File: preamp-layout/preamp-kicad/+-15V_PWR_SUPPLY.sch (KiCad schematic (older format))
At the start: 33 parts, among them J1 Screw_Terminal_01x02, J2 Conn_01x03_Female, J3 Conn_01x03_Female, J4 Conn_01x03_Female, T1 Transformer_1P_1S, U1 L7805, U2 LM7905_TO220

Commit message: AC PCB Update
Removed Switch symbol from PCB, moved to main sheet. Started playing with footprint assignment. Other minor updates.
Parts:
- renumbered J1 to J5, J2 to J6, J3 to J7, J4 to J8
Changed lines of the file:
@@
 $EndDescr
 $Comp
-L Connector:Screw_Terminal_01x02 J1
+L Connector:Screw_Terminal_01x02 J5
 U 1 1 5F8FF1B9
 P 1200 3150
-F 0 "J1" H 1118 3275 50  0000 C CNN
+F 0 "J5" H 1118 3275 50  0000 C CNN
 F 1 "Screw_Terminal_01x02" H 1118 2916 50  0001 C CNN
 F 2 "" H 1200 3150 50  0001 C CNN
@@
 AR Path="/5E2D8DA2/647A815C" Ref="J?"  Part="1"
 AR Path="/6009D432/647A815C" Ref="J?"  Part="1"
-AR Path="/5E27B612/647A815C" Ref="J2"  Part="1"
-F 0 "J2" H 2228 5826 50  0000 L CNN
+AR Path="/5E27B612/647A815C" Ref="J6"  Part="1"
+F 0 "J6" H 2228 5826 50  0000 L CNN
 F 1 "Conn_01x03_Female" H 2228 5735 50  0001 L CNN
 F 2 "" H 2200 5800 50  0001 C CNN
@@
 AR Path="/5E2D8DA2/647B6C33" Ref="J?"  Part="1"
 AR Path="/6009D432/647B6C33" Ref="J?"  Part="1"
-AR Path="/5E27B612/647B6C33" Ref="J3"  Part="1"
-F 0 "J3" H 2228 6426 50  0000 L CNN
+AR Path="/5E27B612/647B6C33" Ref="J7"  Part="1"
+F 0 "J7" H 2228 6426 50  0000 L CNN
 F 1 "Conn_01x03_Female" H 2228 6335 50  0001 L CNN
 F 2 "" H 2200 6400 50  0001 C CNN
@@
 AR Path="/5E2D8DA2/647BAB03" Ref="J?"  Part="1"
 AR Path="/6009D432/647BAB03" Ref="J?"  Part="1"
-AR Path="/5E27B612/647BAB03" Ref="J4"  Part="1"
-F 0 "J4" H 2228 7026 50  0000 L CNN
+AR Path="/5E27B612/647BAB03" Ref="J8"  Part="1"
+F 0 "J8" H 2228 7026 50  0000 L CNN
 F 1 "Conn_01x03_Female" H 2228 6935 50  0001 L CNN
 F 2 "" H 2200 7000 50  0001 C CNN
@@
 $EndComp
 $Comp
-L power:PWR_FLAG #FLG0101
+L power:PWR_FLAG #FLG01
 U 1 1 65A127EB
 P 6800 2050
-F 0 "#FLG0101" H 6800 2125 50  0001 C CNN
+F 0 "#FLG01" H 6800 2125 50  0001 C CNN
 F 1 "PWR_FLAG" H 6800 2223 50  0000 C CNN
 F 2 "" H 6800 2050 50  0001 C CNN
@@
 $EndComp
 $Comp
-L power:PWR_FLAG #FLG0102
+L power:PWR_FLAG #FLG02
 U 1 1 65A13199
 P 6800 4450
-F 0 "#FLG0102" H 6800 4525 50  0001 C CNN
+F 0 "#FLG02" H 6800 4525 50  0001 C CNN
 F 1 "PWR_FLAG" H 6800 4623 50  0000 C CNN
 F 2 "" H 6800 4450 50  0001 C CNN
@@
 	8100 2700 8100 2350
 $Comp
-L power:PWR_FLAG #FLG0103
+L power:PWR_FLAG #FLG03
 U 1 1 65AD6168
 P 8350 2700
-F 0 "#FLG0103" H 8350 2775 50  0001 C CNN
+F 0 "#FLG03" H 8350 2775 50  0001 C CNN
 F 1 "PWR_FLAG" H 8350 2873 50  0000 C CNN
 F 2 "" H 8350 2700 50  0001 C CNN
@@
 Connection ~ 8350 3800
 $Comp
-L power:PWR_FLAG #FLG0104
+L power:PWR_FLAG #FLG04
 U 1 1 65ADBCDE
 P 8350 3800
-F 0 "#FLG0104" H 8350 3875 50  0001 C CNN
+F 0 "#FLG04" H 8350 3875 50  0001 C CNN
 F 1 "PWR_FLAG" H 8350 3973 50  0000 C CNN
 F 2 "" H 8350 3800 50  0001 C CNN

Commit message: Initial Footprint Assignment
Assigned footprints to SMT resistors, pin headers, screw terminals, LEDs, DIP-8 ICs
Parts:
- D2, D3: footprint (none) -> LED_SMD:LED_1206_3216Metric_Pad1.42x1.75mm_HandSolder
- F2: value Fuse -> 500mA
- J5: footprint (none) -> TerminalBlock_Phoenix:TerminalBlock_Phoenix_PT-1,5-2-5.0-H_1x02_P5.00mm_Horizontal
- J6, J7, J8: footprint (none) -> Connector_PinHeader_2.54mm:PinHeader_1x03_P2.54mm_Vertical
- R2, R3: footprint (none) -> Resistor_SMD:R_1206_3216Metric_Pad1.42x1.75mm_HandSolder
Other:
- moved on the sheet: J5
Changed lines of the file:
@@
 L Connector:Screw_Terminal_01x02 J5
 U 1 1 5F8FF1B9
-P 1200 3150
-F 0 "J5" H 1118 3275 50  0000 C CNN
-F 1 "Screw_Terminal_01x02" H 1118 2916 50  0001 C CNN
-F 2 "" H 1200 3150 50  0001 C CNN
-F 3 "~" H 1200 3150 50  0001 C CNN
-	1    1200 3150
+P 1300 3150
+F 0 "J5" H 1218 3275 50  0000 C CNN
+F 1 "Screw_Terminal_01x02" H 1218 2916 50  0001 C CNN
+F 2 "TerminalBlock_Phoenix:TerminalBlock_Phoenix_PT-1,5-2-5.0-H_1x02_P5.00mm_Horizontal" H 1300 3150 50  0001 C CNN
+F 3 "~" H 1300 3150 50  0001 C CNN
+	1    1300 3150
 	-1   0    0    -1
 $EndComp
 Wire Wire Line
-	1400 3150 1500 3150
-Wire Wire Line
 	1800 3150 1800 3000
 Wire Wire Line
-	1400 3250 1600 3250
-Wire Wire Line
 	1800 3250 1800 3400
-Text HLabel 1500 3400 3    50   UnSpc ~ 0
+Text HLabel 1650 3050 1    50   UnSpc ~ 0
 AC+
-Text HLabel 1600 3400 3    50   UnSpc ~ 0
+Text HLabel 1650 3350 3    50   UnSpc ~ 0
 AC-
-Wire Wire Line
-	1500 3400 1500 3150
-Connection ~ 1500 3150
-Wire Wire Line
-	1500 3150 1800 3150
-Wire Wire Line
-	1600 3400 1600 3250
-Connection ~ 1600 3250
-Wire Wire Line
-	1600 3250 1800 3250
 Text GLabel 4550 6200 1    50   UnSpc ~ 0
 +15V
@@
 F 0 "R2" V 4343 6450 50  0000 C CNN
 F 1 "10K" V 4434 6450 50  0000 C CNN
-F 2 "" V 4480 6450 50  0001 C CNN
+F 2 "Resistor_SMD:R_1206_3216Metric_Pad1.42x1.75mm_HandSolder" V 4480 6450 50  0001 C CNN
 F 3 "~" H 4550 6450 50  0001 C CNN
 	1    4550 6450
@@
 F 0 "D2" V 4589 6733 50  0000 R CNN
 F 1 "LED" V 4498 6733 50  0000 R CNN
-F 2 "" H 4550 6850 50  0001 C CNN
+F 2 "LED_SMD:LED_1206_3216Metric_Pad1.42x1.75mm_HandSolder" H 4550 6850 50  0001 C CNN
 F 3 "~" H 4550 6850 50  0001 C CNN
 	1    4550 6850
@@
 F 0 "R3" V 4893 6450 50  0000 C CNN
 F 1 "10K" V 4984 6450 50  0000 C CNN
-F 2 "" V 5030 6450 50  0001 C CNN
+F 2 "Resistor_SMD:R_1206_3216Metric_Pad1.42x1.75mm_HandSolder" V 5030 6450 50  0001 C CNN
 F 3 "~" H 5100 6450 50  0001 C CNN
 	1    5100 6450
@@
 F 0 "D3" V 5139 6733 50  0000 R CNN
 F 1 "LED" V 5048 6733 50  0000 R CNN
-F 2 "" H 5100 6850 50  0001 C CNN
+F 2 "LED_SMD:LED_1206_3216Metric_Pad1.42x1.75mm_HandSolder" H 5100 6850 50  0001 C CNN
 F 3 "~" H 5100 6850 50  0001 C CNN
 	1    5100 6850
@@
 AR Path="/5E27B612/60029A0D" Ref="F2"  Part="1"
 F 0 "F2" V 2603 3000 50  0000 C CNN
-F 1 "Fuse" V 2694 3000 50  0000 C CNN
+F 1 "500mA" V 2694 3000 50  0000 C CNN
 F 2 "" V 2730 3000 50  0001 C CNN
 F 3 "~" H 2800 3000 50  0001 C CNN
@@
 U 1 1 5FD657B8
 P 2200 3200
-F 0 "T1" H 2200 3581 50  0000 C CNN
-F 1 "Transformer_1P_1S" H 2200 3490 50  0000 C CNN
+F 0 "T1" H 2200 3489 50  0000 C CNN
+F 1 "Transformer_1P_1S" H 2200 3490 50  0001 C CNN
 F 2 "" H 2200 3200 50  0001 C CNN
 F 3 "~" H 2200 3200 50  0001 C CNN
@@
 F 0 "J6" H 2228 5826 50  0000 L CNN
 F 1 "Conn_01x03_Female" H 2228 5735 50  0001 L CNN
-F 2 "" H 2200 5800 50  0001 C CNN
+F 2 "Connector_PinHeader_2.54mm:PinHeader_1x03_P2.54mm_Vertical" H 2200 5800 50  0001 C CNN
 F 3 "~" H 2200 5800 50  0001 C CNN
 	1    2200 5800
@@
 F 0 "J7" H 2228 6426 50  0000 L CNN
 F 1 "Conn_01x03_Female" H 2228 6335 50  0001 L CNN
-F 2 "" H 2200 6400 50  0001 C CNN
+F 2 "Connector_PinHeader_2.54mm:PinHeader_1x03_P2.54mm_Vertical" H 2200 6400 50  0001 C CNN
 F 3 "~" H 2200 6400 50  0001 C CNN
 	1    2200 6400
@@
 F 0 "J8" H 2228 7026 50  0000 L CNN
 F 1 "Conn_01x03_Female" H 2228 6935 50  0001 L CNN
-F 2 "" H 2200 7000 50  0001 C CNN
+F 2 "Connector_PinHeader_2.54mm:PinHeader_1x03_P2.54mm_Vertical" H 2200 7000 50  0001 C CNN
 F 3 "~" H 2200 7000 50  0001 C CNN
 	1    2200 7000
@@
 	-1   0    0    1
 $EndComp
+Wire Wire Line
+	1500 3150 1650 3150
+Wire Wire Line
+	1500 3250 1650 3250
+Wire Wire Line
+	1650 3050 1650 3150
+Connection ~ 1650 3150
+Wire Wire Line
+	1650 3150 1800 3150
+Wire Wire Line
+	1650 3250 1650 3350
+Connection ~ 1650 3250
+Wire Wire Line
+	1650 3250 1800 3250
 $EndSCHEMATC

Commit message: BOM update
Minor changes to schematic, value changes and footprint entry. BOM updated with parts sourcing
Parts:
- D4, D5: value D -> SM4001; footprint (none) -> Diode_SMD:D_SOD-123F
- D6, D7: value 1N4004 -> SM4001; footprint (none) -> Diode_SMD:D_SOD-123F
- R2, R3: value 10K -> 430
- R6, R7: value 240R 1% -> 240R
- RV1, RV2: value R_POT_US -> 5k
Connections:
- wire segments 124 -> 122
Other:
- moved on the sheet: D1, F2, J5
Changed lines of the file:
@@
 L Connector:Screw_Terminal_01x02 J5
 U 1 1 5F8FF1B9
-P 1300 3150
-F 0 "J5" H 1218 3275 50  0000 C CNN
-F 1 "Screw_Terminal_01x02" H 1218 2916 50  0001 C CNN
-F 2 "TerminalBlock_Phoenix:TerminalBlock_Phoenix_PT-1,5-2-5.0-H_1x02_P5.00mm_Horizontal" H 1300 3150 50  0001 C CNN
-F 3 "~" H 1300 3150 50  0001 C CNN
-	1    1300 3150
+P 900 3150
+F 0 "J5" H 818 3275 50  0000 C CNN
+F 1 "Screw_Terminal_01x02" H 818 2916 50  0001 C CNN
+F 2 "TerminalBlock_Phoenix:TerminalBlock_Phoenix_PT-1,5-2-5.0-H_1x02_P5.00mm_Horizontal" H 900 3150 50  0001 C CNN
+F 3 "~" H 900 3150 50  0001 C CNN
+	1    900  3150
 	-1   0    0    -1
 $EndComp
@@
 Wire Wire Line
 	1800 3250 1800 3400
-Text HLabel 1650 3050 1    50   UnSpc ~ 0
+Text HLabel 1250 3050 1    50   UnSpc ~ 0
 AC+
-Text HLabel 1650 3350 3    50   UnSpc ~ 0
+Text HLabel 1250 3350 3    50   UnSpc ~ 0
 AC-
 Text GLabel 4550 6200 1    50   UnSpc ~ 0
@@
 AR Path="/5FFF1130" Ref="R?"  Part="1"
 AR Path="/5E27B612/5FFF1130" Ref="R2"  Part="1"
-F 0 "R2" V 4343 6450 50  0000 C CNN
-F 1 "10K" V 4434 6450 50  0000 C CNN
+F 0 "R2" H 4620 6496 50  0000 L CNN
+F 1 "430" H 4620 6405 50  0000 L CNN
 F 2 "Resistor_SMD:R_1206_3216Metric_Pad1.42x1.75mm_HandSolder" V 4480 6450 50  0001 C CNN
 F 3 "~" H 4550 6450 50  0001 C CNN
@@
 AR Path="/5FFF1146" Ref="R?"  Part="1"
 AR Path="/5E27B612/5FFF1146" Ref="R3"  Part="1"
-F 0 "R3" V 4893 6450 50  0000 C CNN
-F 1 "10K" V 4984 6450 50  0000 C CNN
+F 0 "R3" H 5170 6496 50  0000 L CNN
+F 1 "430" H 5170 6405 50  0000 L CNN
 F 2 "Resistor_SMD:R_1206_3216Metric_Pad1.42x1.75mm_HandSolder" V 5030 6450 50  0001 C CNN
 F 3 "~" H 5100 6450 50  0001 C CNN
@@
 AR Path="/5E2D8DA2/5FFF114C" Ref="D?"  Part="1"
 AR Path="/5E27B612/5FFF114C" Ref="D3"  Part="1"
-F 0 "D3" V 5139 6733 50  0000 R CNN
-F 1 "LED" V 5048 6733 50  0000 R CNN
+F 0 "D3" V 5047 6928 50  0000 L CNN
+F 1 "LED" V 5138 6928 50  0000 L CNN
 F 2 "LED_SMD:LED_1206_3216Metric_Pad1.42x1.75mm_HandSolder" H 5100 6850 50  0001 C CNN
 F 3 "~" H 5100 6850 50  0001 C CNN
@@
 L Device:Fuse F?
 U 1 1 60029A0D
-P 2800 3000
+P 1550 3150
 AR Path="/5E26F6FE/60029A0D" Ref="F?"  Part="1"
 AR Path="/5E27B612/60029A0D" Ref="F2"  Part="1"
-F 0 "F2" V 2603 3000 50  0000 C CNN
-F 1 "500mA" V 2694 3000 50  0000 C CNN
-F 2 "" V 2730 3000 50  0001 C CNN
-F 3 "~" H 2800 3000 50  0001 C CNN
-	1    2800 3000
+F 0 "F2" V 1353 3150 50  0000 C CNN
+F 1 "500mA" V 1444 3150 50  0000 C CNN
+F 2 "" V 1480 3150 50  0001 C CNN
+F 3 "~" H 1550 3150 50  0001 C CNN
+	1    1550 3150
 	0    1    1    0
 $EndComp
-Wire Wire Line
-	2600 3000 2650 3000
-Wire Wire Line
-	2600 3400 2650 3400
 $Comp
 L Diode_Bridge:DF02M D1
 U 1 1 5FBF248C
-P 3300 3200
-F 0 "D1" H 3644 3246 50  0000 L CNN
-F 1 "DF02M" H 3644 3155 50  0000 L CNN
-F 2 "Diode_THT:Diode_Bridge_DIP-4_W7.62mm_P5.08mm" H 3450 3325 50  0001 L CNN
-F 3 "http://www.vishay.com/docs/88571/dfm.pdf" H 3300 3200 50  0001 C CNN
-	1    3300 3200
-	1    0    0    -1
-$EndComp
-Wire Wire Line
-	2650 3400 2650 3550
-Wire Wire Line
-	2650 3550 3300 3550
-Wire Wire Line
-	3300 3550 3300 3500
-Wire Wire Line
-	2950 3000 3000 3000
-Wire Wire Line
-	3000 3000 3000 2850
-Wire Wire Line
-	3000 2850 3300 2850
-Wire Wire Line
-	3300 2850 3300 2900
-Wire Wire Line
-	3000 3200 3000 3650
-Wire Wire Line
-	3600 3200 3600 3650
-Text Label 3000 3650 3    50   ~ 0
+P 3150 3200
+F 0 "D1" H 3494 3246 50  0000 L CNN
+F 1 "DF02M" H 3494 3155 50  0000 L CNN
+F 2 "Diode_THT:Diode_Bridge_DIP-4_W7.62mm_P5.08mm" H 3300 3325 50  0001 L CNN
+F 3 "http://www.vishay.com/docs/88571/dfm.pdf" H 3150 3200 50  0001 C CNN
+	1    3150 3200
+	1    0    0    -1
+$EndComp
+Text Label 2850 3800 3    50   ~ 0
 rectified_-
-Text Label 3600 3650 3    50   ~ 0
+Text Label 3450 3800 3    50   ~ 0
 rectified_+
 $Comp
@@
 AR Path="/5E27B612/5FE3F8A6" Ref="D4"  Part="1"
 AR Path="/5E5EF2D4/5FE3F8A6" Ref="D?"  Part="1"
-F 0 "D4" V 8054 1679 50  0000 L CNN
-F 1 "D" V 8145 1679 50  0000 L CNN
-F 2 "" H 8100 1600 50  0001 C CNN
+F 0 "D4" H 8100 1816 50  0000 C CNN
+F 1 "SM4001" H 8100 1725 50  0000 C CNN
+F 2 "Diode_SMD:D_SOD-123F" H 8100 1600 50  0001 C CNN
 F 3 "~" H 8100 1600 50  0001 C CNN
 	1    8100 1600
@@
 AR Path="/5E5EF2D4/5FE3F8AD" Ref="R?"  Part="1"
 F 0 "R6" H 8670 2696 50  0000 L CNN
-F 1 "240R 1%" H 8670 2605 50  0000 L CNN
+F 1 "240R" H 8670 2605 50  0000 L CNN
 F 2 "" V 8530 2650 50  0001 C CNN
 F 3 "~" H 8600 2650 50  0001 C CNN
@@
 AR Path="/5E27B612/5FE3F8C5" Ref="C6"  Part="1"
 AR Path="/5E5EF2D4/5FE3F8C5" Ref="C?"  Part="1"
-F 0 "C6" H 7615 2396 50  0000 L CNN
-F 1 "100nF 35V" H 7615 2305 50  0000 L CNN
+F 0 "C6" H 7386 2396 50  0000 R CNN
+F 1 "100nF 35V" H 7386 2305 50  0000 R CNN
 F 2 "" H 7538 2200 50  0001 C CNN
 F 3 "~" H 7500 2350 50  0001 C CNN
@@
 AR Path="/5E5EF2D4/5FE3F900" Ref="RV?"  Part="1"
 AR Path="/5E27B612/5FE3F900" Ref="RV1"  Part="1"
-F 0 "RV1" H 8033 2996 50  0000 R CNN
-F 1 "R_POT_US" H 8033 2905 50  0000 R CNN
+F 0 "RV1" H 8032 2996 50  0000 R CNN
+F 1 "5k" H 8032 2905 50  0000 R CNN
 F 2 "" H 8100 2950 50  0001 C CNN
 F 3 "~" H 8100 2950 50  0001 C CNN
@@
 AR Path="/5E5EF2D4/5FE3F90F" Ref="D?"  Part="1"
 F 0 "D6" V 9104 2729 50  0000 L CNN
-F 1 "1N4004" V 9195 2729 50  0000 L CNN
-F 2 "" H 9150 2650 50  0001 C CNN
+F 1 "SM4001" V 9195 2729 50  0000 L CNN
+F 2 "Diode_SMD:D_SOD-123F" H 9150 2650 50  0001 C CNN
 F 3 "~" H 9150 2650 50  0001 C CNN
 	1    9150 2650
@@
 AR Path="/5E27B612/5FE3F923" Ref="C9"  Part="1"
 AR Path="/5E5EF2D4/5FE3F923" Ref="C?"  Part="1"
-F 0 "C9" H 9765 3896 50  0000 L CNN
-F 1 "100nF 35V" H 9765 3805 50  0000 L CNN
+F 0 "C9" H 9765 3804 50  0000 L CNN
+F 1 "100nF 35V" H 9765 3895 50  0000 L CNN
 F 2 "" H 9688 3700 50  0001 C CNN
 F 3 "~" H 9650 3850 50  0001 C CNN
@@
 AR Path="/5E27B612/5FE3F929" Ref="D5"  Part="1"
 AR Path="/5E5EF2D4/5FE3F929" Ref="D?"  Part="1"
-F 0 "D5" V 8054 4979 50  0000 L CNN
-F 1 "D" V 8145 4979 50  0000 L CNN
-F 2 "" H 8100 4900 50  0001 C CNN
+F 0 "D5" H 8100 4776 50  0000 C CNN
+F 1 "SM4001" H 8100 4685 50  0000 C CNN
+F 2 "Diode_SMD:D_SOD-123F" H 8100 4900 50  0001 C CNN
 F 3 "~" H 8100 4900 50  0001 C CNN
 	1    8100 4900
@@
 AR Path="/5E27B612/5FE3F930" Ref="R7"  Part="1"
 AR Path="/5E5EF2D4/5FE3F930" Ref="R?"  Part="1"
-F 0 "R7" H 8670 3896 50  0000 L CNN
-F 1 "240R 1%" H 8670 3805 50  0000 L CNN
+F 0 "R7" H 8670 3804 50  0000 L CNN
+F 1 "240R" H 8670 3895 50  0000 L CNN
 F 2 "" V 8530 3850 50  0001 C CNN
 F 3 "~" H 8600 3850 50  0001 C CNN
@@
 AR Path="/5E27B612/5FE3F93A" Ref="R5"  Part="1"
 AR Path="/5E5EF2D4/5FE3F93A" Ref="R?"  Part="1"
-F 0 "R5" V 6193 4450 50  0000 C CNN
-F 1 "10R 1W" V 6284 4450 50  0000 C CNN
+F 0 "R5" V 6607 4450 50  0000 C CNN
+F 1 "10R 1W" V 6516 4450 50  0000 C CNN
 F 2 "" V 6330 4450 50  0001 C CNN
 F 3 "~" H 6400 4450 50  0001 C CNN
@@
 AR Path="/5E5EF2D4/5FE3F975" Ref="RV?"  Part="1"
 AR Path="/5E27B612/5FE3F975" Ref="RV2"  Part="1"
-F 0 "RV2" H 8033 3596 50  0000 R CNN
-F 1 "R_POT_US" H 8033 3505 50  0000 R CNN
+F 0 "RV2" H 8032 3504 50  0000 R CNN
+F 1 "5k" H 8032 3595 50  0000 R CNN
 F 2 "" H 8100 3550 50  0001 C CNN
 F 3 "~" H 8100 3550 50  0001 C CNN
@@
 AR Path="/5E5EF2D4/5FE3F992" Ref="D?"  Part="1"
 F 0 "D7" V 9104 3771 50  0000 R CNN
-F 1 "1N4004" V 9195 3771 50  0000 R CNN
-F 2 "" H 9150 3850 50  0001 C CNN
+F 1 "SM4001" V 9195 3771 50  0000 R CNN
+F 2 "Diode_SMD:D_SOD-123F" H 9150 3850 50  0001 C CNN
 F 3 "~" H 9150 3850 50  0001 C CNN
 	1    9150 3850
@@
 AR Path="/6009D432/647A815C" Ref="J?"  Part="1"
 AR Path="/5E27B612/647A815C" Ref="J6"  Part="1"
-F 0 "J6" H 2228 5826 50  0000 L CNN
+F 0 "J6" H 2228 5780 50  0000 L CNN
 F 1 "Conn_01x03_Female" H 2228 5735 50  0001 L CNN
 F 2 "Connector_PinHeader_2.54mm:PinHeader_1x03_P2.54mm_Vertical" H 2200 5800 50  0001 C CNN
@@
 AR Path="/6009D432/647B6C33" Ref="J?"  Part="1"
 AR Path="/5E27B612/647B6C33" Ref="J7"  Part="1"
-F 0 "J7" H 2228 6426 50  0000 L CNN
+F 0 "J7" H 2228 6380 50  0000 L CNN
 F 1 "Conn_01x03_Female" H 2228 6335 50  0001 L CNN
 F 2 "Connector_PinHeader_2.54mm:PinHeader_1x03_P2.54mm_Vertical" H 2200 6400 50  0001 C CNN
@@
 AR Path="/6009D432/647BAB03" Ref="J?"  Part="1"
 AR Path="/5E27B612/647BAB03" Ref="J8"  Part="1"
-F 0 "J8" H 2228 7026 50  0000 L CNN
+F 0 "J8" H 2228 6980 50  0000 L CNN
 F 1 "Conn_01x03_Female" H 2228 6935 50  0001 L CNN
 F 2 "Connector_PinHeader_2.54mm:PinHeader_1x03_P2.54mm_Vertical" H 2200 7000 50  0001 C CNN
@@
 AR Path="/5E27B612/64A0321E" Ref="#PWR06"  Part="1"
 F 0 "#PWR06" H 1900 6750 50  0001 C CNN
-F 1 "GND" H 1905 6827 50  0000 C CNN
+F 1 "GND" V 1905 6872 50  0000 R CNN
 F 2 "" H 1900 7000 50  0001 C CNN
 F 3 "" H 1900 7000 50  0001 C CNN
@@
 AR Path="/5E27B612/64A1966F" Ref="#PWR05"  Part="1"
 F 0 "#PWR05" H 1900 6150 50  0001 C CNN
-F 1 "GND" H 1905 6227 50  0000 C CNN
+F 1 "GND" V 1905 6272 50  0000 R CNN
 F 2 "" H 1900 6400 50  0001 C CNN
 F 3 "" H 1900 6400 50  0001 C CNN
@@
 AR Path="/5E27B612/64A1D9A5" Ref="#PWR04"  Part="1"
 F 0 "#PWR04" H 1900 5550 50  0001 C CNN
-F 1 "GND" H 1905 5627 50  0000 C CNN
+F 1 "GND" V 1905 5672 50  0000 R CNN
 F 2 "" H 1900 5800 50  0001 C CNN
 F 3 "" H 1900 5800 50  0001 C CNN
@@
 $EndComp
 Wire Wire Line
-	1500 3150 1650 3150
-Wire Wire Line
-	1500 3250 1650 3250
-Wire Wire Line
-	1650 3050 1650 3150
-Connection ~ 1650 3150
-Wire Wire Line
-	1650 3150 1800 3150
-Wire Wire Line
-	1650 3250 1650 3350
-Connection ~ 1650 3250
-Wire Wire Line
-	1650 3250 1800 3250
+	1100 3150 1250 3150
+Wire Wire Line
+	1100 3250 1250 3250
+Wire Wire Line
+	1250 3050 1250 3150
+Connection ~ 1250 3150
+Wire Wire Line
+	1250 3250 1250 3350
+Connection ~ 1250 3250
+Wire Wire Line
+	1250 3150 1400 3150
+Wire Wire Line
+	1250 3250 1800 3250
+Wire Wire Line
+	1700 3150 1800 3150
+Wire Wire Line
+	3150 2900 3150 2800
+Wire Wire Line
+	3150 2800 2600 2800
+Wire Wire Line
+	2600 2800 2600 3000
+Wire Wire Line
+	2600 3650 2600 3400
+Wire Wire Line
+	3150 3500 3150 3650
+Wire Wire Line
+	2600 3650 3150 3650
+Wire Wire Line
+	2850 3800 2850 3200
+Wire Wire Line
+	3450 3200 3450 3800
 $EndSCHEMATC

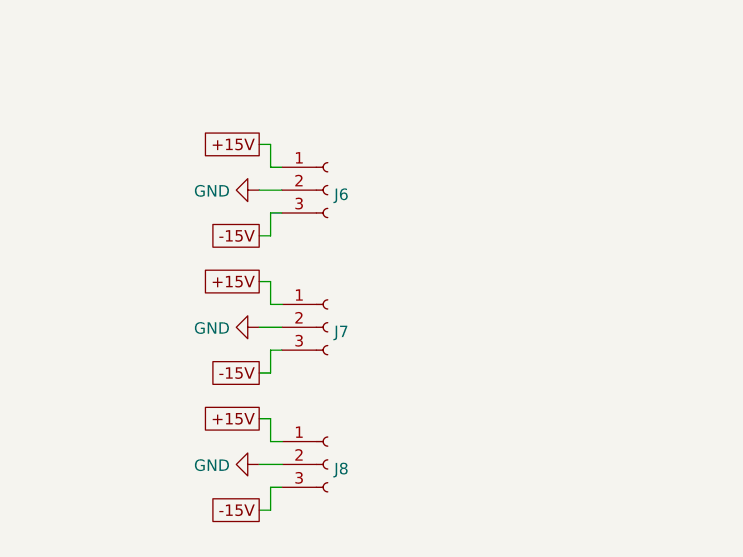
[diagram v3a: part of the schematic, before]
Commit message: power headers updated, slight BOM update
changed footprint on all 5V, +-15V to JST B2B / B3B connectors. All male conns now.
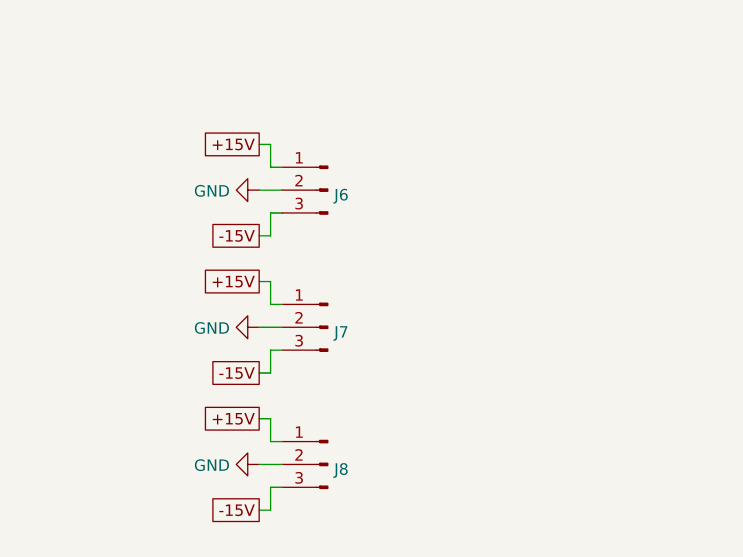
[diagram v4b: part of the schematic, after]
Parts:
- removed J6, J7, J8: Conn_01x03_Female, Connector_PinHeader_2.54mm:PinHeader_1x03_P2.54mm_Vertical, symbol Connector:Conn_01x03_Female
- added J6, J7, J8: Conn_01x03_Male, Connector_JST:JST_EH_B3B-EH-A_1x03_P2.50mm_Vertical, symbol Connector:Conn_01x03_Male
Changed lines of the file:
@@
 	6000 4450 5800 4450
 Connection ~ 6000 4450
-$Comp
-L Connector:Conn_01x03_Female J?
-U 1 1 647A815C
-P 2200 5800
-AR Path="/5E607732/647A815C" Ref="J?"  Part="1"
-AR Path="/5E2D8DA2/647A815C" Ref="J?"  Part="1"
-AR Path="/6009D432/647A815C" Ref="J?"  Part="1"
-AR Path="/5E27B612/647A815C" Ref="J6"  Part="1"
-F 0 "J6" H 2228 5780 50  0000 L CNN
-F 1 "Conn_01x03_Female" H 2228 5735 50  0001 L CNN
-F 2 "Connector_PinHeader_2.54mm:PinHeader_1x03_P2.54mm_Vertical" H 2200 5800 50  0001 C CNN
-F 3 "~" H 2200 5800 50  0001 C CNN
-	1    2200 5800
-	1    0    0    -1
-$EndComp
 Text GLabel 1900 5600 0    50   UnSpc ~ 0
 +15V
@@
 Wire Wire Line
 	1950 6000 1900 6000
-$Comp
-L Connector:Conn_01x03_Female J?
-U 1 1 647B6C33
-P 2200 6400
-AR Path="/5E607732/647B6C33" Ref="J?"  Part="1"
-AR Path="/5E2D8DA2/647B6C33" Ref="J?"  Part="1"
-AR Path="/6009D432/647B6C33" Ref="J?"  Part="1"
-AR Path="/5E27B612/647B6C33" Ref="J7"  Part="1"
-F 0 "J7" H 2228 6380 50  0000 L CNN
-F 1 "Conn_01x03_Female" H 2228 6335 50  0001 L CNN
-F 2 "Connector_PinHeader_2.54mm:PinHeader_1x03_P2.54mm_Vertical" H 2200 6400 50  0001 C CNN
-F 3 "~" H 2200 6400 50  0001 C CNN
-	1    2200 6400
-	1    0    0    -1
-$EndComp
 Text GLabel 1900 6200 0    50   UnSpc ~ 0
 +15V
@@
 Wire Wire Line
 	1950 6600 1900 6600
-$Comp
-L Connector:Conn_01x03_Female J?
-U 1 1 647BAB03
-P 2200 7000
-AR Path="/5E607732/647BAB03" Ref="J?"  Part="1"
-AR Path="/5E2D8DA2/647BAB03" Ref="J?"  Part="1"
-AR Path="/6009D432/647BAB03" Ref="J?"  Part="1"
-AR Path="/5E27B612/647BAB03" Ref="J8"  Part="1"
-F 0 "J8" H 2228 6980 50  0000 L CNN
-F 1 "Conn_01x03_Female" H 2228 6935 50  0001 L CNN
-F 2 "Connector_PinHeader_2.54mm:PinHeader_1x03_P2.54mm_Vertical" H 2200 7000 50  0001 C CNN
-F 3 "~" H 2200 7000 50  0001 C CNN
-	1    2200 7000
-	1    0    0    -1
-$EndComp
 Text GLabel 1900 6800 0    50   UnSpc ~ 0
 +15V
@@
 Wire Wire Line
 	3450 3200 3450 3800
+$Comp
+L Connector:Conn_01x03_Male J6
+U 1 1 5E5A9FCF
+P 2200 5800
+AR Path="/5E27B612/5E5A9FCF" Ref="J6"  Part="1"
+AR Path="/6009D432/5E5A9FCF" Ref="J?"  Part="1"
+AR Path="/5E1A0CE1/5E5A9FCF" Ref="J?"  Part="1"
+F 0 "J6" H 2172 5778 50  0000 R CNN
+F 1 "Conn_01x03_Male" H 2172 5733 50  0001 R CNN
+F 2 "Connector_JST:JST_EH_B3B-EH-A_1x03_P2.50mm_Vertical" H 2200 5800 50  0001 C CNN
+F 3 "~" H 2200 5800 50  0001 C CNN
+	1    2200 5800
+	-1   0    0    -1
+$EndComp
+$Comp
+L Connector:Conn_01x03_Male J7
+U 1 1 5E5BC88E
+P 2200 6400
+AR Path="/5E27B612/5E5BC88E" Ref="J7"  Part="1"
+AR Path="/6009D432/5E5BC88E" Ref="J?"  Part="1"
+AR Path="/5E1A0CE1/5E5BC88E" Ref="J?"  Part="1"
+F 0 "J7" H 2172 6378 50  0000 R CNN
+F 1 "Conn_01x03_Male" H 2172 6333 50  0001 R CNN
+F 2 "Connector_JST:JST_EH_B3B-EH-A_1x03_P2.50mm_Vertical" H 2200 6400 50  0001 C CNN
+F 3 "~" H 2200 6400 50  0001 C CNN
+	1    2200 6400
+	-1   0    0    -1
+$EndComp
+$Comp
+L Connector:Conn_01x03_Male J8
+U 1 1 5E5C1243
+P 2200 7000
+AR Path="/5E27B612/5E5C1243" Ref="J8"  Part="1"
+AR Path="/6009D432/5E5C1243" Ref="J?"  Part="1"
+AR Path="/5E1A0CE1/5E5C1243" Ref="J?"  Part="1"
+F 0 "J8" H 2172 6978 50  0000 R CNN
+F 1 "Conn_01x03_Male" H 2172 6933 50  0001 R CNN
+F 2 "Connector_JST:JST_EH_B3B-EH-A_1x03_P2.50mm_Vertical" H 2200 7000 50  0001 C CNN
+F 3 "~" H 2200 7000 50  0001 C CNN
+	1    2200 7000
+	-1   0    0    -1
+$EndComp
 $EndSCHEMATC
